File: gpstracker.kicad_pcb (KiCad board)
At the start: 2 copper layers, 79.2 x 59.2 mm, 205 parts, among them IC1 SIM808, J1 Molex 105133-0002, J2 Leds, J3 47553-0001, J4 CONN_COAXIAL, J5 CONN_COAXIAL, J6 Micro_SD_Card, Q1 DMP1045U, SW1 Reset, U1 MCP73832-5-OT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

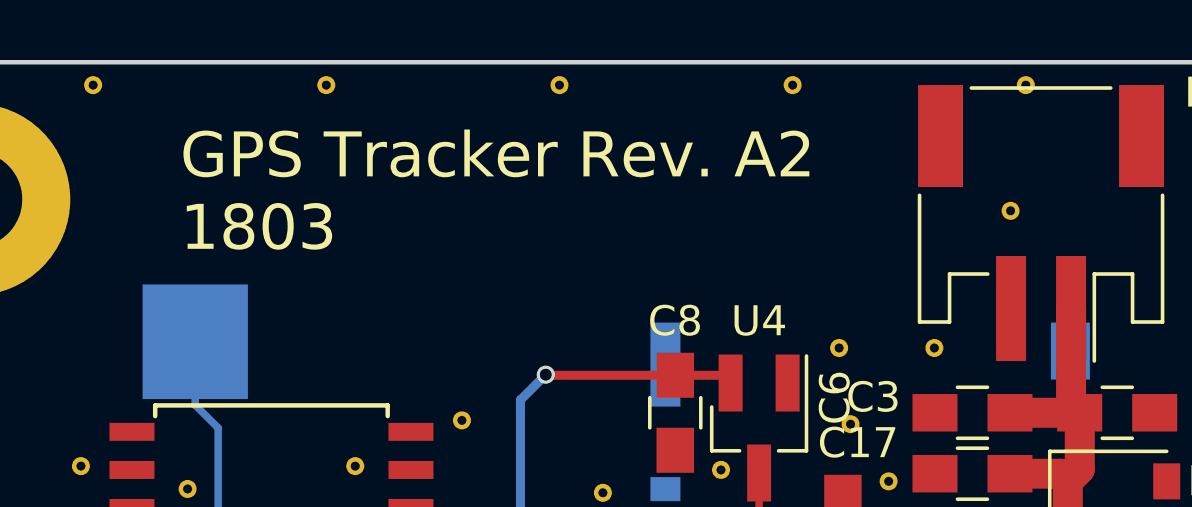
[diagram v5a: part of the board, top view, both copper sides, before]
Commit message: Reported last changes from schematics to PCB
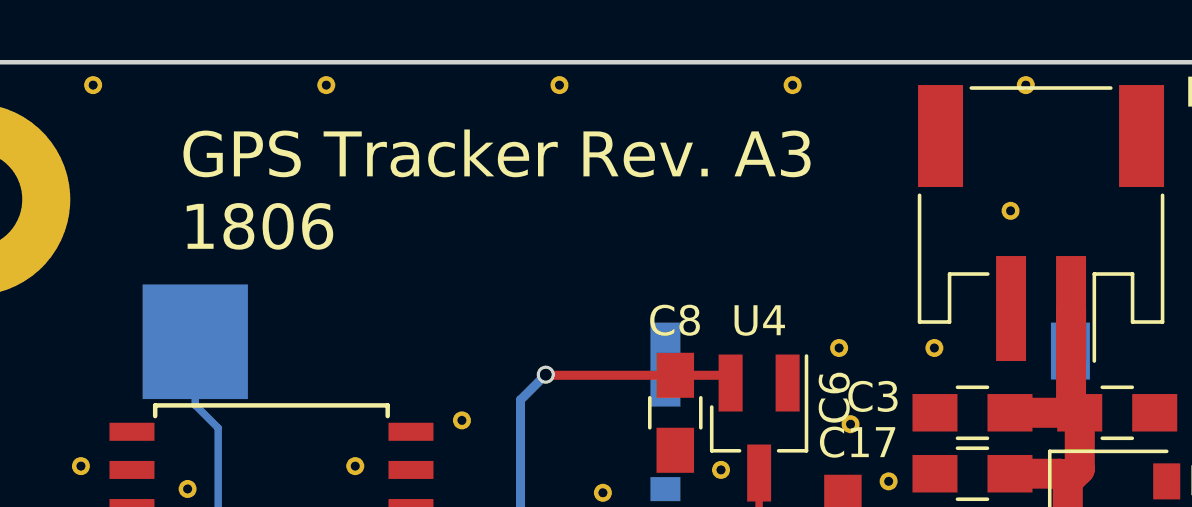
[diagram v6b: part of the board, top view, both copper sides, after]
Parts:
- U1: value MCP73832-5-OT -> MCP73831-2-OT
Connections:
- U3 pad 7: Net-(U3-Pad7) -> GND
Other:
- board text added: "GPS Tracker Rev. A3 1806"
- board text removed: "GPS Tracker Rev. A2 1803"
